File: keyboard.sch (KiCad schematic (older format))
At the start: 84 parts, among them IC1 ATMEGA32U4, J1 MINI, P1 CONN_1, P10 CONN_1, P11 CONN_1, P12 CONN_1, P13 CONN_1, P14 CONN_1, P15 CONN_1, P16 CONN_1, P17 CONN_1, P18 CONN_1, P19 CONN_1, P2 CONN_1, P20 CONN_1, P21 CONN_1, P22 CONN_1, P23 CONN_1, P24 CONN_1, P25 CONN_1, P26 CONN_1, P27 CONN_1, P28 CONN_1, P29 CONN_1, P3 CONN_1, P30 CONN_1, P31 CONN_1, P32 CONN_1, P33 CONN_1, P34 CONN_1, P35 CONN_1, P36 CONN_1, P37 CONN_1, P38 CONN_1, P39 CONN_1, P4 CONN_1, P40 CONN_1, P41 CONN_1, P42 CONN_1, P5 CONN_1, P6 CONN_1, P7 CONN_1, P8 CONN_1, P9 CONN_1, X1 ASX3F

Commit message: Remap project symbols
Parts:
- C1, C2, C3, C4, C5, C6, C7, C8: symbol C -> device:C
- DF10, DF11, DF20, DF201, DF21, DF211, DF22, DF221, DF23, DF231, DF232, DF3, DW1, DW2, DW3, DW4: symbol LED -> device:LED
- IC1: symbol ATMEGA32U4 -> atmega32u4:ATMEGA32U4
- J1: symbol USBMINI_B05 -> oupiin_usb:USBMINI_B05
- P1, P10, P11, P12, P13, P14, P15, P16, P17, P18, P19, P2, P20, P21, P22, P23, P24, P25, P26, P27, P28, P29, P3, P30, P31, P32, P33, P34, P35, P36, P37, P38, P39, P4, P40, P41, P42, P5, P6, P7, P8, P9: symbol CONN_1 -> conn:CONN_1
- R1, R10, R11, R12, R13, R14, R15, R2, R3, R5, R6, R7, R8, R9: symbol R -> device:R
- S0: symbol DTSM-6 -> dtsjw:DTSM-6
- X1: symbol ASX4 -> aker:ASX4
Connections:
- wire segments 205 -> 245

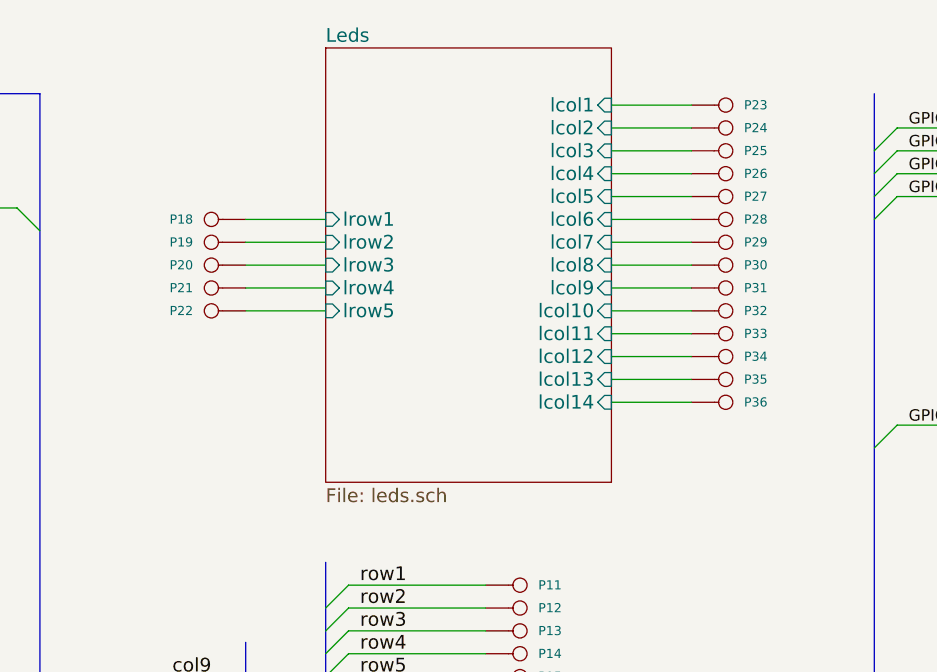
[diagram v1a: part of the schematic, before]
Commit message: Delete leds from schematic
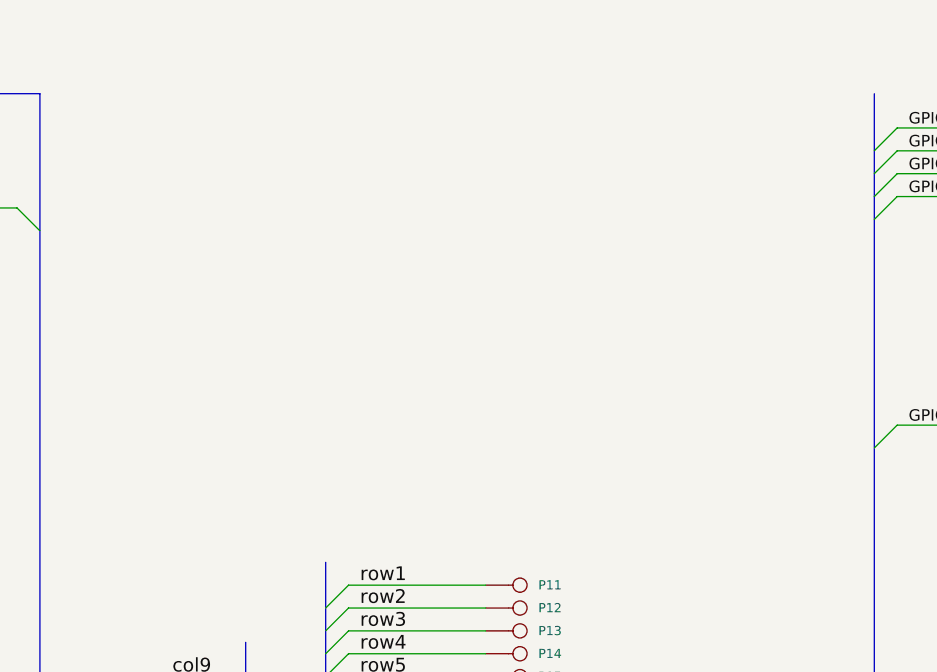
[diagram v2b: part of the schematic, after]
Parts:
- removed P18, P19, P20, P21, P22, P23, P24, P25, P26, P27, P28, P29, P30, P31, P32, P33, P34, P35, P36: CONN_1, symbol conn:CONN_1
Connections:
- wire segments 245 -> 226

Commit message: Associate missing footprints
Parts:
- DF21, DF211, DF22, DF221, DF23, DF231, DF232: footprint (none) -> mx1a:MX1A-led_no3d
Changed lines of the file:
@@
 F 0 "DF21" H 9800 3350 50  0000 L CNN
 F 1 "LED" H 10600 3250 50  0000 C CNN
-F 2 "" H 10450 3350 60  0001 C CNN
+F 2 "mx1a:MX1A-led_no3d" H 10450 3350 60  0001 C CNN
 F 3 "" H 10450 3350 60  0001 C CNN
 	1    10450 3350
@@
 F 0 "DF22" H 9800 3100 50  0000 L CNN
 F 1 "LED" H 10600 3000 50  0000 C CNN
-F 2 "" H 10450 3100 60  0001 C CNN
+F 2 "mx1a:MX1A-led_no3d" H 10450 3100 60  0001 C CNN
 F 3 "" H 10450 3100 60  0001 C CNN
 	1    10450 3100
@@
 F 0 "DF23" H 9800 2850 50  0000 L CNN
 F 1 "LED" H 10600 2750 50  0000 C CNN
-F 2 "" H 10450 2850 60  0001 C CNN
+F 2 "mx1a:MX1A-led_no3d" H 10450 2850 60  0001 C CNN
 F 3 "" H 10450 2850 60  0001 C CNN
 	1    10450 2850
@@
 F 0 "DF211" H 9750 3250 50  0000 L CNN
 F 1 "LED" H 10600 3150 50  0000 C CNN
-F 2 "" H 10450 3250 60  0001 C CNN
+F 2 "mx1a:MX1A-led_no3d" H 10450 3250 60  0001 C CNN
 F 3 "" H 10450 3250 60  0001 C CNN
 	1    10450 3250
@@
 F 0 "DF221" H 9750 3000 50  0000 L CNN
 F 1 "LED" H 10600 2900 50  0000 C CNN
-F 2 "" H 10450 3000 60  0001 C CNN
+F 2 "mx1a:MX1A-led_no3d" H 10450 3000 60  0001 C CNN
 F 3 "" H 10450 3000 60  0001 C CNN
 	1    10450 3000
@@
 F 0 "DF231" H 9750 2750 50  0000 L CNN
 F 1 "LED" H 10600 2650 50  0000 C CNN
-F 2 "" H 10450 2750 60  0001 C CNN
+F 2 "mx1a:MX1A-led_no3d" H 10450 2750 60  0001 C CNN
 F 3 "" H 10450 2750 60  0001 C CNN
 	1    10450 2750
@@
 F 0 "DF232" H 9750 2650 50  0000 L CNN
 F 1 "LED" H 10600 2550 50  0000 C CNN
-F 2 "" H 10450 2650 60  0001 C CNN
+F 2 "mx1a:MX1A-led_no3d" H 10450 2650 60  0001 C CNN
 F 3 "" H 10450 2650 60  0001 C CNN
 	1    10450 2650

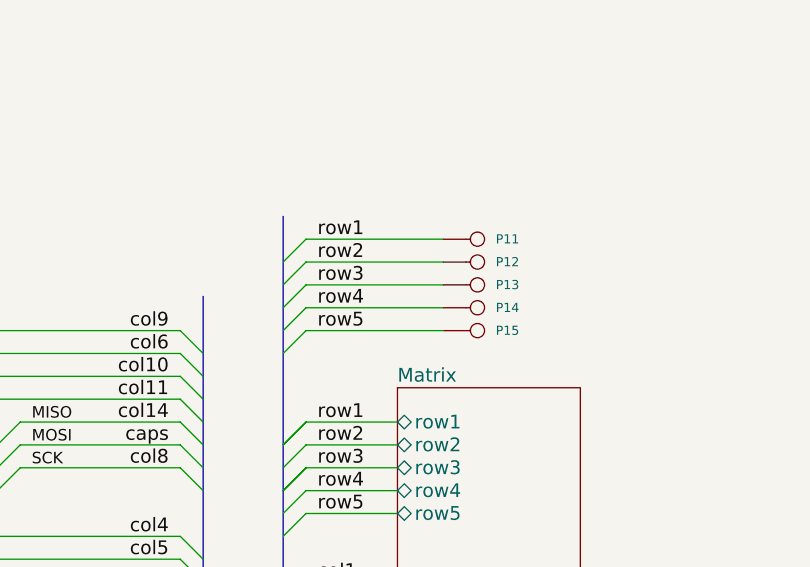
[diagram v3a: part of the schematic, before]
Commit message: New PCB layout for bottom, left, mod4, mod5 and mod6
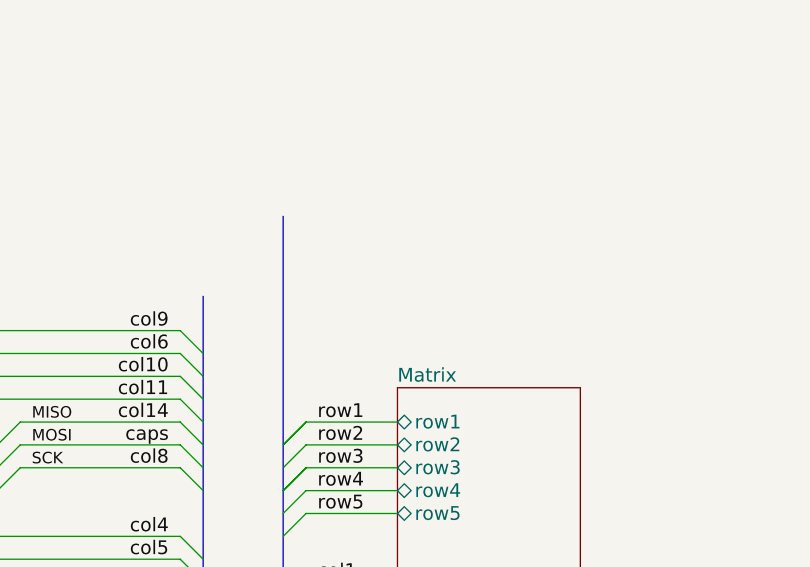
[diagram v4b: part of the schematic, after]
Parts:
- removed P11, P12, P13, P14, P15: CONN_1, symbol conn:CONN_1
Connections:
- wire segments 226 -> 221
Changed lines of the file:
@@
 GPIO3
-$Comp
-L conn:CONN_1 P11
-U 1 1 51365814
-P 7400 3050
-F 0 "P11" H 7480 3050 40  0000 L CNN
-F 1 "CONN_1" H 7400 3105 30  0001 C CNN
-F 2 "" H 7400 3050 60  0001 C CNN
-F 3 "" H 7400 3050 60  0001 C CNN
-	1    7400 3050
-	1    0    0    -1
-$EndComp
-$Comp
-L conn:CONN_1 P12
-U 1 1 5136581A
-P 7400 3150
-F 0 "P12" H 7480 3150 40  0000 L CNN
-F 1 "CONN_1" H 7400 3205 30  0001 C CNN
-F 2 "" H 7400 3150 60  0001 C CNN
-F 3 "" H 7400 3150 60  0001 C CNN
-	1    7400 3150
-	1    0    0    -1
-$EndComp
-$Comp
-L conn:CONN_1 P13
-U 1 1 51365820
-P 7400 3250
-F 0 "P13" H 7480 3250 40  0000 L CNN
-F 1 "CONN_1" H 7400 3305 30  0001 C CNN
-F 2 "" H 7400 3250 60  0001 C CNN
-F 3 "" H 7400 3250 60  0001 C CNN
-	1    7400 3250
-	1    0    0    -1
-$EndComp
-$Comp
-L conn:CONN_1 P14
-U 1 1 51365826
-P 7400 3350
-F 0 "P14" H 7480 3350 40  0000 L CNN
-F 1 "CONN_1" H 7400 3405 30  0001 C CNN
-F 2 "" H 7400 3350 60  0001 C CNN
-F 3 "" H 7400 3350 60  0001 C CNN
-	1    7400 3350
-	1    0    0    -1
-$EndComp
-$Comp
-L conn:CONN_1 P15
-U 1 1 51365868
-P 7400 3450
-F 0 "P15" H 7480 3450 40  0000 L CNN
-F 1 "CONN_1" H 7400 3505 30  0001 C CNN
-F 2 "" H 7400 3450 60  0001 C CNN
-F 3 "" H 7400 3450 60  0001 C CNN
-	1    7400 3450
-	1    0    0    -1
-$EndComp
-Entry Wire Line
-	6550 3150 6650 3050
-Entry Wire Line
-	6550 3250 6650 3150
-Entry Wire Line
-	6550 3350 6650 3250
-Entry Wire Line
-	6550 3450 6650 3350
-Entry Wire Line
-	6550 3550 6650 3450
-Text Label 6700 3050 0    60   ~ 0
-row1
-Text Label 6700 3150 0    60   ~ 0
-row2
-Text Label 6700 3250 0    60   ~ 0
-row3
-Text Label 6700 3350 0    60   ~ 0
-row4
-Text Label 6700 3450 0    60   ~ 0
-row5
 $Comp
 L conn:CONN_1 P16
@@
 	9650 5650 9050 5650
 Wire Wire Line
-	6650 3050 7250 3050
-Wire Wire Line
-	7250 3150 6650 3150
-Wire Wire Line
-	6650 3250 7250 3250
-Wire Wire Line
-	6650 3350 7250 3350
-Wire Wire Line
-	7250 3450 6650 3450
-Wire Wire Line
 	9650 5850 9300 5850

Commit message: Remove GPIOs
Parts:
- removed DF10, DF11, DF20, DF201, DF21, DF211, DF22, DF221, DF23, DF231, DF232, DF3, DW1, DW2, DW3, DW4: LED, mx1a:MX1A-led_no3d, symbol device:LED
- removed P10, P16, P17, P37, P38, P39, P40, P41, P42, P7, P8, P9: CONN_1, symbol conn:CONN_1
- removed R10, R11, R12, R13, R14, R15, R6, R7, R8, R9: R, symbol device:R
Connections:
- net labels removed: GPIO0, GPIO1, GPIO2, GPIO3
- wire segments 221 -> 117
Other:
- note removed: "Backlight expansion\nconnector (top)"
- note removed: "Universal expansion\nconnector (bottom)"
